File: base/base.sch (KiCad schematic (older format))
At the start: 18 parts, among them J1 FTDI, J2 CONN_01X04, J3 CONN_01X40, J4 CONN_01X08, SW1 SW_Push, U1 Z80CPU, U2 27C256, U3 7404, U4 55257, U5 7432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

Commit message: Fixed board cutout
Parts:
- removed J2: CONN_01X04, Pin_Headers:Pin_Header_Straight_1x04_Pitch2.54mm, symbol CONN_01X04
- removed J3: CONN_01X40, Pin_Headers:Pin_Header_Straight_1x40_Pitch2.54mm, symbol CONN_01X40
- added J?: CONN_01X40, symbol CONN_01X40
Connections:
- wire segments 235 -> 229

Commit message: Replaced main header with 2x20
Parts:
- removed J4: CONN_01X08, Pin_Headers:Pin_Header_Straight_1x08_Pitch2.54mm, symbol CONN_01X08
- J3: renamed from J?; footprint (none) -> Pin_Headers:Pin_Header_Straight_2x20_Pitch2.54mm
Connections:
- wire segments 229 -> 226
- no-connect marks 3 -> 4

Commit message: Added barrel jack
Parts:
- added J2: Barrel_Jack, Connectors:BARREL_JACK, symbol Barrel_Jack
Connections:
- net +5V: now also J2.1
- net GND: now also J2.2, J2.3
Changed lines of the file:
@@
 	5800 7750 5900 7650
 $Comp
-L GND #PWR022
+L GND #PWR021
 U 1 1 59F6444E
 P 5850 7950
-F 0 "#PWR022" H 5850 7700 50  0001 C CNN
+F 0 "#PWR021" H 5850 7700 50  0001 C CNN
 F 1 "GND" H 5855 7777 50  0000 C CNN
 F 2 "" H 5850 7950 50  0001 C CNN
@@
 $EndComp
 $Comp
-L +5V #PWR023
+L +5V #PWR022
 U 1 1 59F6487C
 P 5700 7750
-F 0 "#PWR023" H 5700 7600 50  0001 C CNN
+F 0 "#PWR022" H 5700 7600 50  0001 C CNN
 F 1 "+5V" H 5715 7923 50  0000 C CNN
 F 2 "" H 5700 7750 50  0001 C CNN
@@
 	6050 7900 5850 7900
 NoConn ~ 11650 3100
+$Comp
+L Barrel_Jack J2
+U 1 1 5A004908
+P 13650 7350
+F 0 "J2" H 13728 7675 50  0000 C CNN
+F 1 "Barrel_Jack" H 13728 7584 50  0000 C CNN
+F 2 "Connectors:BARREL_JACK" H 13700 7310 50  0001 C CNN
+F 3 "" H 13700 7310 50  0001 C CNN
+	1    13650 7350
+	1    0    0    -1
+$EndComp
+$Comp
+L GND #PWR023
+U 1 1 5A004CBD
+P 14050 7550
+F 0 "#PWR023" H 14050 7300 50  0001 C CNN
+F 1 "GND" H 14055 7377 50  0000 C CNN
+F 2 "" H 14050 7550 50  0001 C CNN
+F 3 "" H 14050 7550 50  0001 C CNN
+	1    14050 7550
+	1    0    0    -1
+$EndComp
+Wire Wire Line
+	13950 7350 14050 7350
+Wire Wire Line
+	14050 7350 14050 7550
+Wire Wire Line
+	13950 7450 14050 7450
+Connection ~ 14050 7450
+$Comp
+L +5V #PWR024
+U 1 1 5A004F82
+P 14050 7150
+F 0 "#PWR024" H 14050 7000 50  0001 C CNN
+F 1 "+5V" H 14065 7323 50  0000 C CNN
+F 2 "" H 14050 7150 50  0001 C CNN
+F 3 "" H 14050 7150 50  0001 C CNN
+	1    14050 7150
+	1    0    0    -1
+$EndComp
+Wire Wire Line
+	14050 7150 14050 7250
+Wire Wire Line
+	14050 7250 13950 7250
 $EndSCHEMATC

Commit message: Added regulation to input voltage
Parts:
- added C2, C4: 1 uF, Capacitors_SMD:C_0603, symbol C_Small
- added U7: MIC5205-5.0, TO_SOT_Packages_SMD:SOT-23-5, symbol MIC5205-5.0
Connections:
- net +5V: now also C4.1, U7.5 (OUT); no longer J2.1
- net GND: now also C2.2, C4.2, U7.2 (GND)
- new net: C2.1, J2.1, U7.1 (IN), U7.3 (EN)
- no-connect marks 4 -> 5
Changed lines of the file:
@@
 	6150 3350 6250 3450
 $Comp
-L GND #PWR01
+L GND #PWR4
 U 1 1 5966AA78
 P 2500 5500
-F 0 "#PWR01" H 2500 5250 50  0001 C CNN
+F 0 "#PWR4" H 2500 5250 50  0001 C CNN
 F 1 "GND" H 2505 5327 50  0000 C CNN
 F 2 "" H 2500 5500 50  0001 C CNN
@@
 $EndComp
 $Comp
-L +5V #PWR02
+L +5V #PWR3
 U 1 1 5966ABCC
 P 2500 2000
-F 0 "#PWR02" H 2500 1850 50  0001 C CNN
+F 0 "#PWR3" H 2500 1850 50  0001 C CNN
 F 1 "+5V" H 2515 2173 50  0000 C CNN
 F 2 "" H 2500 2000 50  0001 C CNN
@@
 $EndComp
 $Comp
-L GND #PWR03
+L GND #PWR6
 U 1 1 5966AD0D
 P 5250 4650
-F 0 "#PWR03" H 5250 4400 50  0001 C CNN
+F 0 "#PWR6" H 5250 4400 50  0001 C CNN
 F 1 "GND" H 5255 4477 50  0000 C CNN
 F 2 "" H 5250 4650 50  0001 C CNN
@@
 $EndComp
 $Comp
-L +5V #PWR04
+L +5V #PWR5
 U 1 1 5966ADF6
 P 5250 2150
-F 0 "#PWR04" H 5250 2000 50  0001 C CNN
+F 0 "#PWR5" H 5250 2000 50  0001 C CNN
 F 1 "+5V" H 5265 2323 50  0000 C CNN
 F 2 "" H 5250 2150 50  0001 C CNN
@@
 $EndComp
 $Comp
-L +5V #PWR05
+L +5V #PWR1
 U 1 1 5966B631
 P 950 2600
-F 0 "#PWR05" H 950 2450 50  0001 C CNN
+F 0 "#PWR1" H 950 2450 50  0001 C CNN
 F 1 "+5V" H 965 2773 50  0000 C CNN
 F 2 "" H 950 2600 50  0001 C CNN
@@
 NoConn ~ 650  3000
 $Comp
-L GND #PWR06
+L GND #PWR2
 U 1 1 5966B6FC
 P 950 3400
-F 0 "#PWR06" H 950 3150 50  0001 C CNN
+F 0 "#PWR2" H 950 3150 50  0001 C CNN
 F 1 "GND" H 955 3227 50  0000 C CNN
 F 2 "" H 950 3400 50  0001 C CNN
@@
 $EndComp
 $Comp
-L GND #PWR07
+L GND #PWR18
 U 1 1 5966D26A
 P 12150 8950
-F 0 "#PWR07" H 12150 8700 50  0001 C CNN
+F 0 "#PWR18" H 12150 8700 50  0001 C CNN
 F 1 "GND" H 12155 8777 50  0000 C CNN
 F 2 "" H 12150 8950 50  0001 C CNN
@@
 $EndComp
 $Comp
-L +5V #PWR08
+L +5V #PWR20
 U 1 1 5966D324
 P 13050 8150
-F 0 "#PWR08" H 13050 8000 50  0001 C CNN
+F 0 "#PWR20" H 13050 8000 50  0001 C CNN
 F 1 "+5V" H 13065 8323 50  0000 C CNN
 F 2 "" H 13050 8150 50  0001 C CNN
@@
 ~RESET~
 $Comp
-L GND #PWR09
+L GND #PWR19
 U 1 1 5966DD94
 P 12650 9300
-F 0 "#PWR09" H 12650 9050 50  0001 C CNN
+F 0 "#PWR19" H 12650 9050 50  0001 C CNN
 F 1 "GND" H 12655 9127 50  0000 C CNN
 F 2 "" H 12650 9300 50  0001 C CNN
@@
 $EndComp
 $Comp
-L GND #PWR010
+L GND #PWR22
 U 1 1 5966E3B1
 P 13500 9200
-F 0 "#PWR010" H 13500 8950 50  0001 C CNN
+F 0 "#PWR22" H 13500 8950 50  0001 C CNN
 F 1 "GND" H 13505 9027 50  0000 C CNN
 F 2 "" H 13500 9200 50  0001 C CNN
@@
 $EndComp
 $Comp
-L +5V #PWR011
+L +5V #PWR21
 U 1 1 5966E548
 P 13500 8500
-F 0 "#PWR011" H 13500 8350 50  0001 C CNN
+F 0 "#PWR21" H 13500 8350 50  0001 C CNN
 F 1 "+5V" H 13515 8673 50  0000 C CNN
 F 2 "" H 13500 8500 50  0001 C CNN
@@
 $EndComp
 $Comp
-L +5V #PWR012
+L +5V #PWR9
 U 1 1 5967000D
 P 7500 2200
-F 0 "#PWR012" H 7500 2050 50  0001 C CNN
+F 0 "#PWR9" H 7500 2050 50  0001 C CNN
 F 1 "+5V" H 7515 2373 50  0000 C CNN
 F 2 "" H 7500 2200 50  0001 C CNN
@@
 $EndComp
 $Comp
-L GND #PWR013
+L GND #PWR10
 U 1 1 5967079F
 P 7500 4700
-F 0 "#PWR013" H 7500 4450 50  0001 C CNN
+F 0 "#PWR10" H 7500 4450 50  0001 C CNN
 F 1 "GND" H 7505 4527 50  0000 C CNN
 F 2 "" H 7500 4700 50  0001 C CNN
@@
 $EndComp
 $Comp
-L +5V #PWR014
+L +5V #PWR15
 U 1 1 5967680A
 P 9800 2100
-F 0 "#PWR014" H 9800 1950 50  0001 C CNN
+F 0 "#PWR15" H 9800 1950 50  0001 C CNN
 F 1 "+5V" H 9815 2273 50  0000 C CNN
 F 2 "" H 9800 2100 50  0001 C CNN
@@
 $EndComp
 $Comp
-L GND #PWR015
+L GND #PWR16
 U 1 1 59676BF3
 P 9800 6000
-F 0 "#PWR015" H 9800 5750 50  0001 C CNN
+F 0 "#PWR16" H 9800 5750 50  0001 C CNN
 F 1 "GND" H 9805 5827 50  0000 C CNN
 F 2 "" H 9800 6000 50  0001 C CNN
@@
 NoConn ~ 8800 4700
 $Comp
-L +5V #PWR016
+L +5V #PWR13
 U 1 1 596A671B
 P 8300 3950
-F 0 "#PWR016" H 8300 3800 50  0001 C CNN
+F 0 "#PWR13" H 8300 3800 50  0001 C CNN
 F 1 "+5V" H 8315 4123 50  0000 C CNN
 F 2 "" H 8300 3950 50  0001 C CNN
@@
 $EndComp
 $Comp
-L +5V #PWR017
+L +5V #PWR11
 U 1 1 596A8FB6
 P 7650 5700
-F 0 "#PWR017" H 7650 5550 50  0001 C CNN
+F 0 "#PWR11" H 7650 5550 50  0001 C CNN
 F 1 "+5V" H 7665 5873 50  0000 C CNN
 F 2 "" H 7650 5700 50  0001 C CNN
@@
 NoConn ~ 7350 6100
 $Comp
-L GND #PWR018
+L GND #PWR12
 U 1 1 596A8FBD
 P 7650 6500
-F 0 "#PWR018" H 7650 6250 50  0001 C CNN
+F 0 "#PWR12" H 7650 6250 50  0001 C CNN
 F 1 "GND" H 7655 6327 50  0000 C CNN
 F 2 "" H 7650 6500 50  0001 C CNN
@@
 A15
 $Comp
-L GND #PWR019
+L GND #PWR14
 U 1 1 596AAB37
 P 8450 5550
-F 0 "#PWR019" H 8450 5300 50  0001 C CNN
+F 0 "#PWR14" H 8450 5300 50  0001 C CNN
 F 1 "GND" H 8455 5377 50  0000 C CNN
 F 2 "" H 8450 5550 50  0001 C CNN
@@
 $EndComp
 $Comp
-L GND #PWR020
+L GND #PWR17
 U 1 1 5987A0C1
 P 11750 3400
-F 0 "#PWR020" H 11750 3150 50  0001 C CNN
+F 0 "#PWR17" H 11750 3150 50  0001 C CNN
 F 1 "GND" H 11755 3227 50  0000 C CNN
 F 2 "" H 11750 3400 50  0001 C CNN
@@
 	5800 7750 5900 7650
 $Comp
-L GND #PWR021
+L GND #PWR8
 U 1 1 59F6444E
 P 5850 7950
-F 0 "#PWR021" H 5850 7700 50  0001 C CNN
+F 0 "#PWR8" H 5850 7700 50  0001 C CNN
 F 1 "GND" H 5855 7777 50  0000 C CNN
 F 2 "" H 5850 7950 50  0001 C CNN
@@
 $EndComp
 $Comp
-L +5V #PWR022
+L +5V #PWR7
 U 1 1 59F6487C
 P 5700 7750
-F 0 "#PWR022" H 5700 7600 50  0001 C CNN
+F 0 "#PWR7" H 5700 7600 50  0001 C CNN
 F 1 "+5V" H 5715 7923 50  0000 C CNN
 F 2 "" H 5700 7750 50  0001 C CNN
@@
 $EndComp
 $Comp
-L GND #PWR023
+L GND #PWR23
 U 1 1 5A004CBD
 P 14050 7550
-F 0 "#PWR023" H 14050 7300 50  0001 C CNN
+F 0 "#PWR23" H 14050 7300 50  0001 C CNN
 F 1 "GND" H 14055 7377 50  0000 C CNN
 F 2 "" H 14050 7550 50  0001 C CNN
@@
 Connection ~ 14050 7450
 $Comp
-L +5V #PWR024
+L +5V #PWR25
 U 1 1 5A004F82
-P 14050 7150
-F 0 "#PWR024" H 14050 7000 50  0001 C CNN
-F 1 "+5V" H 14065 7323 50  0000 C CNN
-F 2 "" H 14050 7150 50  0001 C CNN
-F 3 "" H 14050 7150 50  0001 C CNN
-	1    14050 7150
+P 15400 7200
+F 0 "#PWR25" H 15400 7050 50  0001 C CNN
+F 1 "+5V" H 15415 7373 50  0000 C CNN
+F 2 "" H 15400 7200 50  0001 C CNN
+F 3 "" H 15400 7200 50  0001 C CNN
+	1    15400 7200
 	1    0    0    -1
 $EndComp
@@
 	14050 7150 14050 7250
 Wire Wire Line
-	14050 7250 13950 7250
+	13950 7250 14550 7250
+$Comp
+L MIC5205-5.0 U7
+U 1 1 5A00F5FE
+P 14850 7350
+F 0 "U7" H 14850 7692 50  0000 C CNN
+F 1 "MIC5205-5.0" H 14850 7601 50  0000 C CNN
+F 2 "TO_SOT_Packages_SMD:SOT-23-5" H 14850 7675 50  0001 C CNN
+F 3 "" H 14850 7350 50  0001 C CNN
+	1    14850 7350
+	1    0    0    -1
+$EndComp
+Connection ~ 14050 7250
+Wire Wire Line
+	14500 7250 14500 7350
+Wire Wire Line
+	14500 7350 14550 7350
+Connection ~ 14500 7250
+$Comp
+L GND #PWR24
+U 1 1 5A00F976
+P 14850 7750
+F 0 "#PWR24" H 14850 7500 50  0001 C CNN
+F 1 "GND" H 14855 7577 50  0000 C CNN
+F 2 "" H 14850 7750 50  0001 C CNN
+F 3 "" H 14850 7750 50  0001 C CNN
+	1    14850 7750
+	1    0    0    -1
+$EndComp
+Wire Wire Line
+	14850 7650 14850 7750
+Wire Wire Line
+	15150 7250 15400 7250
+Wire Wire Line
+	15400 7250 15400 7200
+$Comp
+L C_Small C2
+U 1 1 5A00FC8F
+P 14350 7400
+F 0 "C2" H 14442 7446 50  0000 L CNN
+F 1 "1 uF" H 14442 7355 50  0000 L CNN
+F 2 "Capacitors_SMD:C_0603" H 14350 7400 50  0001 C CNN
+F 3 "" H 14350 7400 50  0001 C CNN
+	1    14350 7400
+	1    0    0    -1
+$EndComp
+Connection ~ 14050 7500
+NoConn ~ 15150 7350
+$Comp
+L C_Small C4
+U 1 1 5A00FF9B
+P 15300 7400
+F 0 "C4" H 15392 7446 50  0000 L CNN
+F 1 "1 uF" H 15392 7355 50  0000 L CNN
+F 2 "Capacitors_SMD:C_0603" H 15300 7400 50  0001 C CNN
+F 3 "" H 15300 7400 50  0001 C CNN
+	1    15300 7400
+	1    0    0    -1
+$EndComp
+Wire Wire Line
+	15300 7300 15300 7250
+Connection ~ 15300 7250
+Wire Wire Line
+	15300 7700 15300 7500
+Wire Wire Line
+	14350 7700 15300 7700
+Connection ~ 14850 7700
+Wire Wire Line
+	14350 7300 14350 7250
+Connection ~ 14350 7250
+Wire Wire Line
+	14350 7500 14350 7700
 $EndSCHEMATC

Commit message: Fixed capacitor sizes
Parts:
- C1: value 1 uF -> .1 uF; footprint Capacitors_THT:C_Disc_D4.3mm_W1.9mm_P5.00mm -> Capacitors_THT:C_Disc_D4.7mm_W2.5mm_P5.00mm
- C5: value C_Small -> .1 uF; footprint Capacitors_THT:C_Disc_D4.3mm_W1.9mm_P5.00mm -> Capacitors_THT:C_Disc_D4.7mm_W2.5mm_P5.00mm
- R1: footprint Resistors_THT:R_Axial_DIN0207_L6.3mm_D2.5mm_P10.16mm_Horizontal -> Resistors_THT:R_Axial_DIN0207_L6.3mm_D2.5mm_P7.62mm_Horizontal
- SW1: footprint Buttons_Switches_THT:SW_PUSH_6mm_h5mm -> Buttons_Switches_THT:SW_Tactile_SPST_Angled_PTS645Vx31-2LFS

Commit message: Increased size of voltage regulator
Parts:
- removed C2, C4: 1 uF, Capacitors_SMD:C_0603, symbol C_Small
- removed U7: MIC5205-5.0, TO_SOT_Packages_SMD:SOT-23-5, symbol MIC5205-5.0
- added C2, C4: 10 uF, Capacitors_SMD:C_1206, symbol CP_Small
- added U7: AP1117-50, TO_SOT_Packages_SMD:SOT-223-3Lead_TabPin2, symbol AP1117-50
- C1: value .1 uF -> 1 uF
- C5: value .1 uF -> C_Small
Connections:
- net +5V: now also C4.1, U7.2 (VO)
- net GND: now also C2.2, C4.2, U7.1 (GND)
- net at J2.1: now also C2.1, U7.3 (VI)
- no-connect marks 5 -> 4

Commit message: Fixed decoupling caps
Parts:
- C5: value C_Small -> .1 uF
- U1: symbol Z80CPU -> Z80CPU-RESCUE-base
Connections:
- net +5V: now also C1.2, U1.11 (VCC), U6.40 (VCC); no longer C1.1
- net GND: now also C1.1, C5.2
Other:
- moved on the sheet: C1, C5
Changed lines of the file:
@@
-EESchema Schematic File Version 2
+EESchema Schematic File Version 3
+LIBS:base-rescue
 LIBS:power
 LIBS:device
@@
 $EndDescr
 $Comp
-L Z80CPU U1
+L Z80CPU-RESCUE-base U1
 U 1 1 59669CB9
 P 2500 3900
@@
 L C_Small C1
 U 1 1 5966AFCC
-P 2500 2200
-F 0 "C1" H 2592 2246 50  0000 L CNN
-F 1 "1 uF" H 2592 2155 50  0000 L CNN
-F 2 "Capacitors_THT:C_Disc_D4.7mm_W2.5mm_P5.00mm" H 2500 2200 50  0001 C CNN
-F 3 "" H 2500 2200 50  0001 C CNN
-	1    2500 2200
-	1    0    0    -1
+P 2300 2200
+F 0 "C1" H 2392 2246 50  0000 L CNN
+F 1 "1 uF" H 2392 2155 50  0000 L CNN
+F 2 "Capacitors_THT:C_Disc_D4.7mm_W2.5mm_P5.00mm" H 2300 2200 50  0001 C CNN
+F 3 "" H 2300 2200 50  0001 C CNN
+	1    2300 2200
+	0    -1   -1   0
 $EndComp
 $Comp
@@
 L C_Small C5
 U 1 1 59676716
-P 9800 2300
-F 0 "C5" H 9892 2346 50  0000 L CNN
-F 1 "C_Small" H 9892 2255 50  0000 L CNN
-F 2 "Capacitors_THT:C_Disc_D4.7mm_W2.5mm_P5.00mm" H 9800 2300 50  0001 C CNN
-F 3 "" H 9800 2300 50  0001 C CNN
-	1    9800 2300
-	1    0    0    -1
+P 9600 2300
+F 0 "C5" H 9692 2346 50  0000 L CNN
+F 1 ".1 uF" H 9692 2255 50  0000 L CNN
+F 2 "Capacitors_THT:C_Disc_D4.7mm_W2.5mm_P5.00mm" H 9600 2300 50  0001 C CNN
+F 3 "" H 9600 2300 50  0001 C CNN
+	1    9600 2300
+	0    1    1    0
 $EndComp
 $Comp
@@
 	9800 5900 9800 6000
 Wire Wire Line
-	9800 2100 9800 2200
-Wire Wire Line
-	9800 2400 9800 2500
+	9800 2100 9800 2500
 Wire Wire Line
 	8800 2800 8600 2800
@@
 	2500 5400 2500 5500
 Wire Wire Line
-	2500 2300 2500 2400
+	2500 2000 2500 2400
 Wire Wire Line
 	5250 4550 5250 4650
-Wire Wire Line
-	2500 2000 2500 2100
 Wire Wire Line
 	5250 2150 5250 2550
@@
 Wire Wire Line
 	14350 7250 14350 7300
+$Comp
+L GND #PWR026
+U 1 1 5A0E3541
+P 2100 2300
+F 0 "#PWR026" H 2100 2050 50  0001 C CNN
+F 1 "GND" H 2105 2127 50  0000 C CNN
+F 2 "" H 2100 2300 50  0001 C CNN
+F 3 "" H 2100 2300 50  0001 C CNN
+	1    2100 2300
+	1    0    0    -1
+$EndComp
+Wire Wire Line
+	2100 2300 2100 2200
+Wire Wire Line
+	2100 2200 2200 2200
+Wire Wire Line
+	2400 2200 2500 2200
+Connection ~ 2500 2200
+Wire Wire Line
+	9700 2300 9800 2300
+Connection ~ 9800 2300
+$Comp
+L GND #PWR027
+U 1 1 5A0E45B0
+P 9400 2400
+F 0 "#PWR027" H 9400 2150 50  0001 C CNN
+F 1 "GND" H 9405 2227 50  0000 C CNN
+F 2 "" H 9400 2400 50  0001 C CNN
+F 3 "" H 9400 2400 50  0001 C CNN
+	1    9400 2400
+	1    0    0    -1
+$EndComp
+Wire Wire Line
+	9400 2400 9400 2300
+Wire Wire Line
+	9400 2300 9500 2300
 $EndSCHEMATC

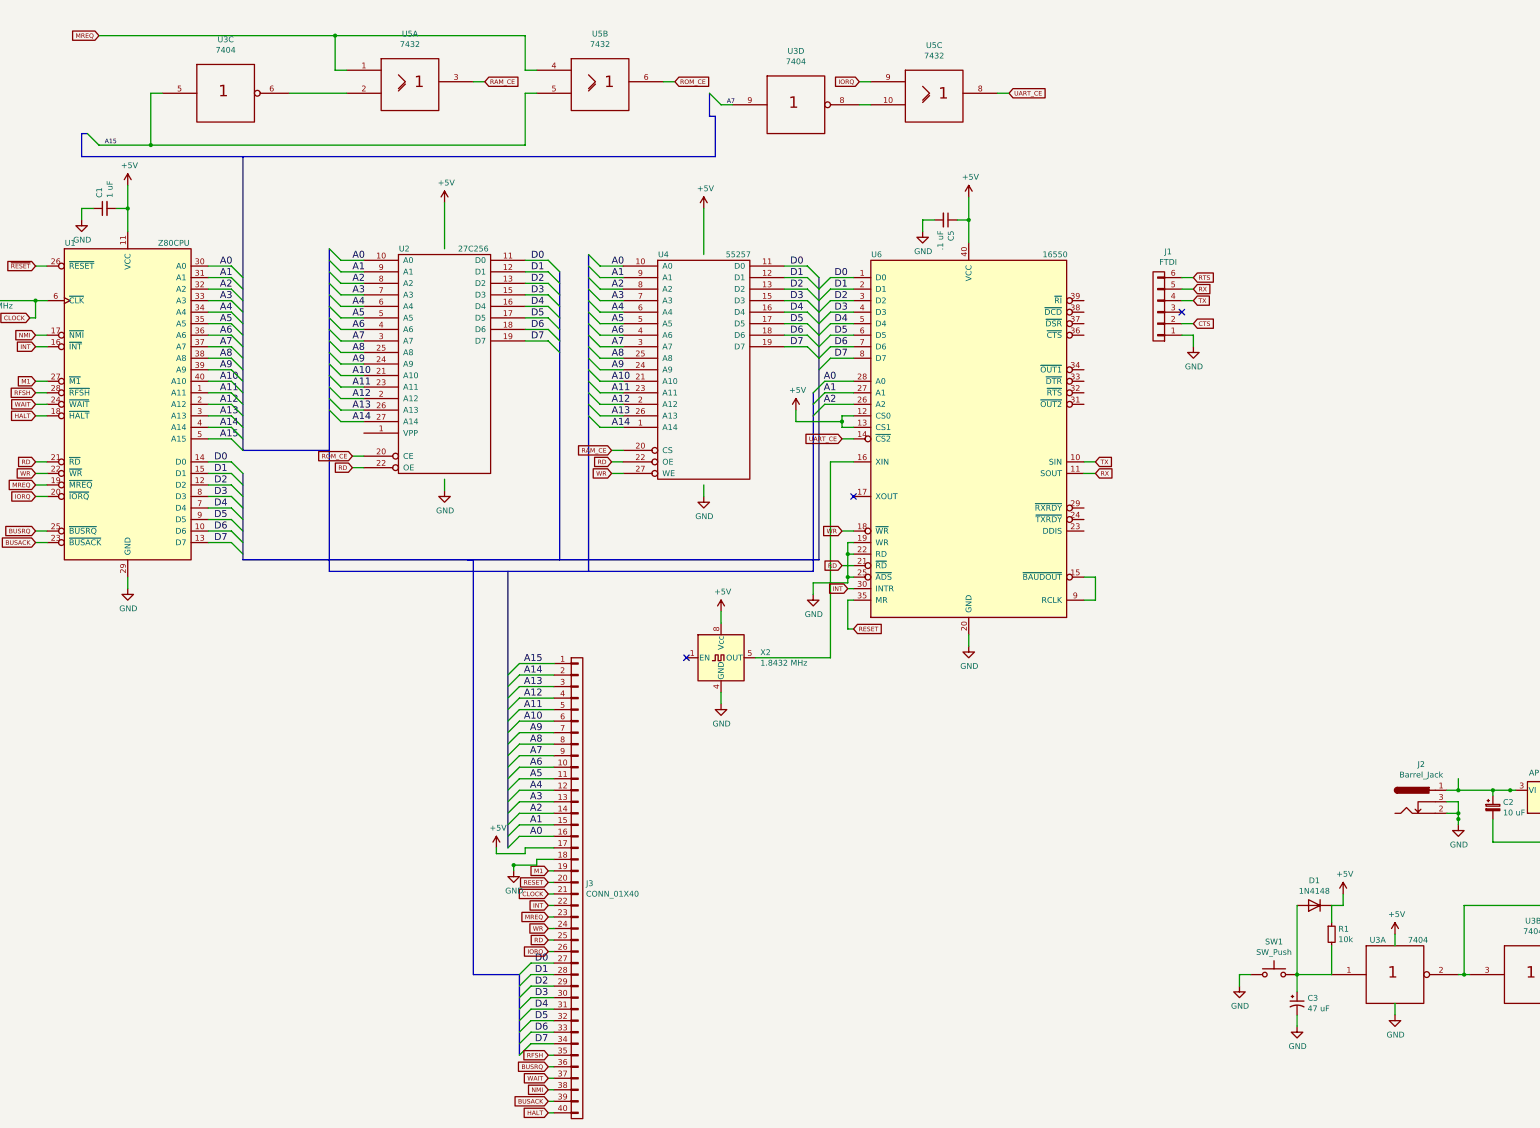
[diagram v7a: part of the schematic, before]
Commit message: Clean up schematic and added more decoupling
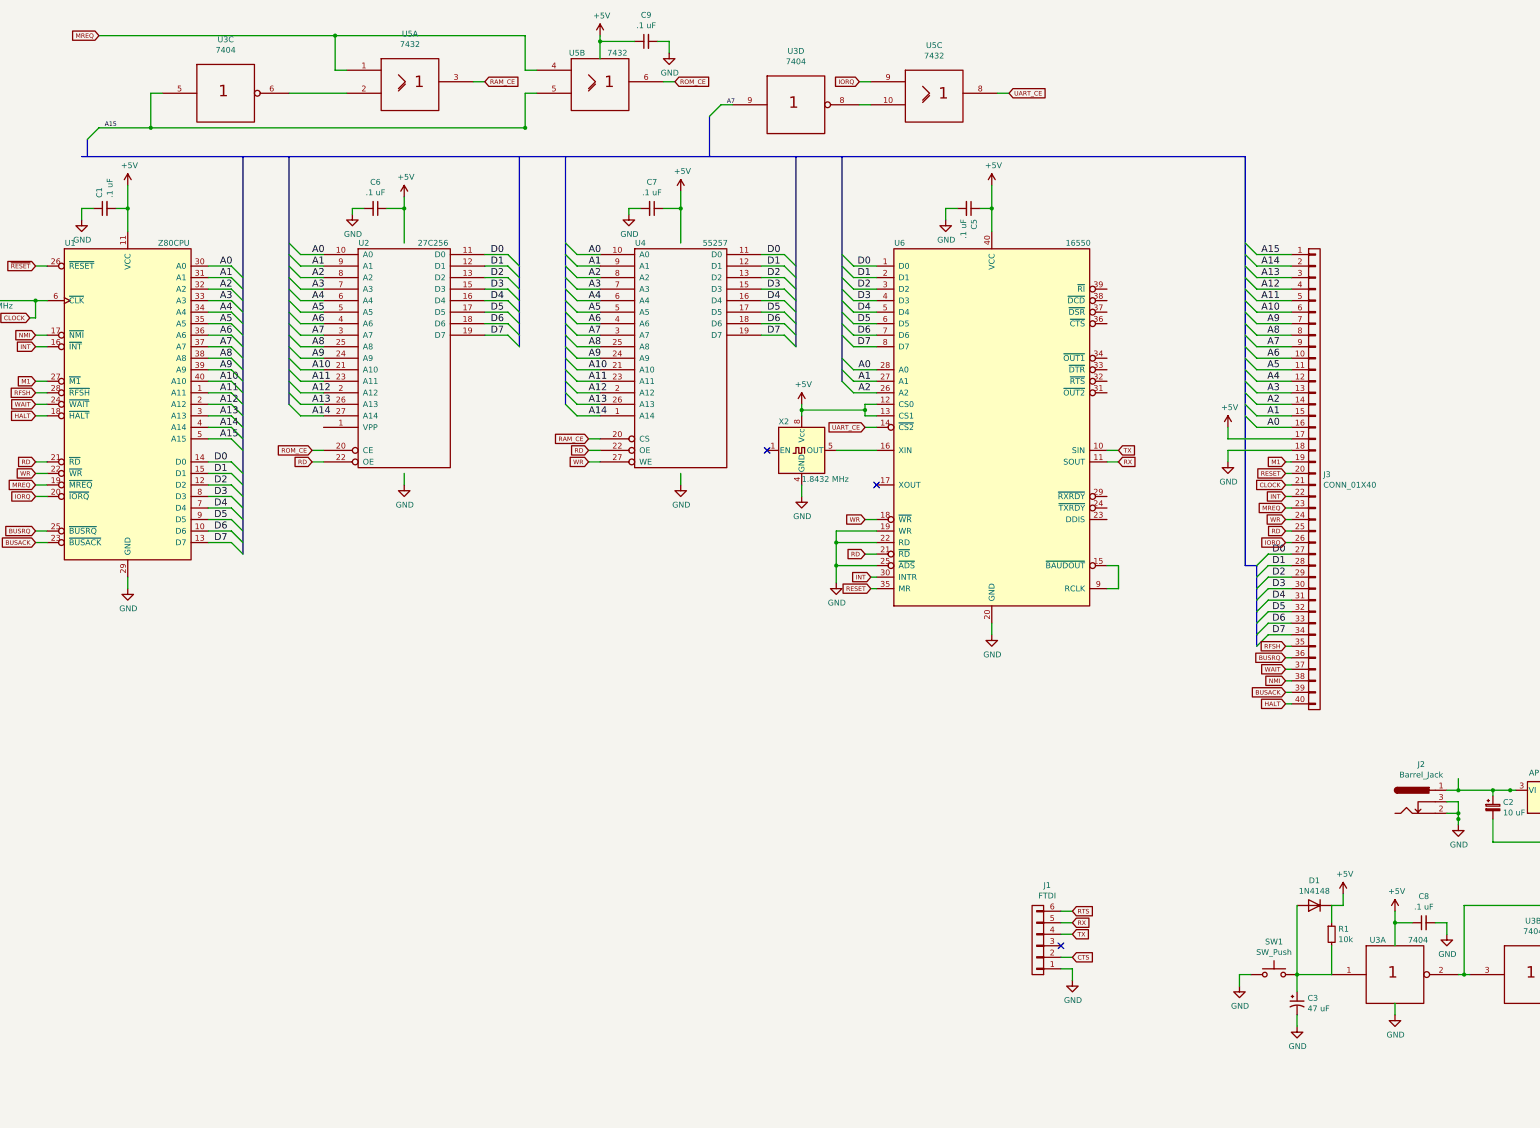
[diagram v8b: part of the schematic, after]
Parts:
- added C6, C7, C8, C9: .1 uF, Capacitors_THT:C_Disc_D4.7mm_W2.5mm_P5.00mm, symbol C_Small
- C1: value 1 uF -> .1 uF
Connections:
- net +5V: now also C6.1, C7.1, C8.1, C9.1
- net GND: now also C6.2, C7.2, C8.2, C9.2
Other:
- moved on the sheet: C5, J1, J3, U2, U4, U6, X2
